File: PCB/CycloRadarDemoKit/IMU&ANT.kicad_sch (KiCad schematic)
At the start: 18 parts, among them J101 ANT_SWD, U302 D52MxxM8, U402 MPU-6050

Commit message: JLCPCB mistakes repaired, cosmetics on PCB
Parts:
- C103: LCSC C14663 -> (none)
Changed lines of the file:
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@@
-      (effects (font (size 1.27 1.27)) hide)
-    )
-    (property "LCSC" "C14663" (at 121.92 57.15 0)
       (effects (font (size 1.27 1.27)) hide)
     )

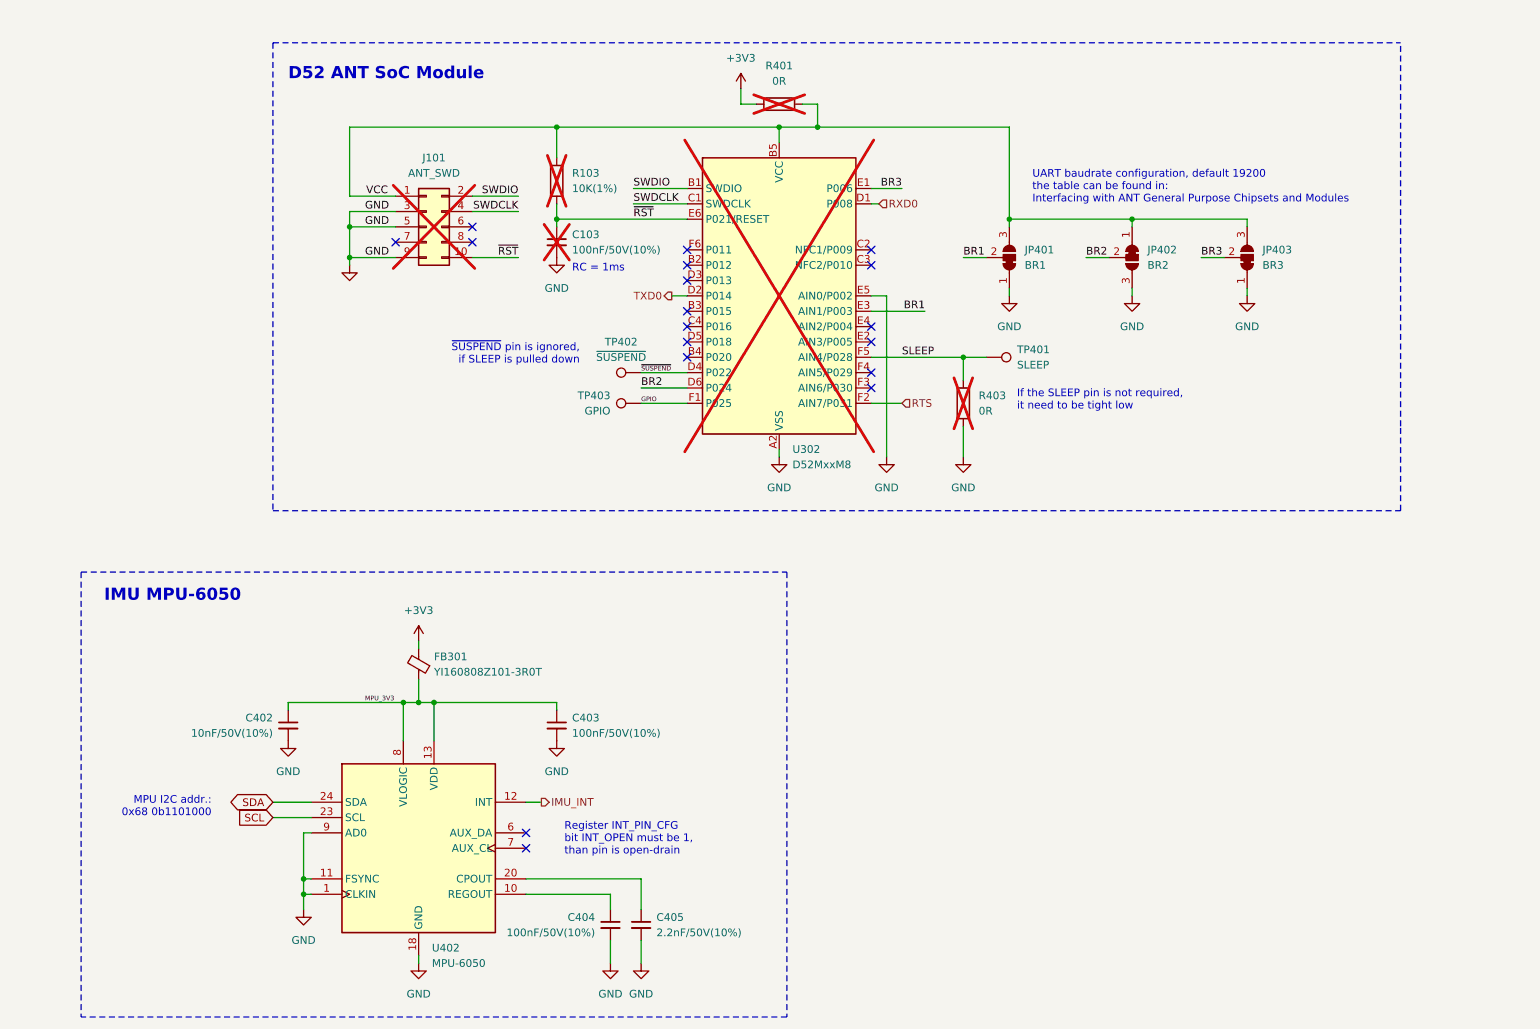
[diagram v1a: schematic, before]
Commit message: Sematic Versioning implemented, whish list added
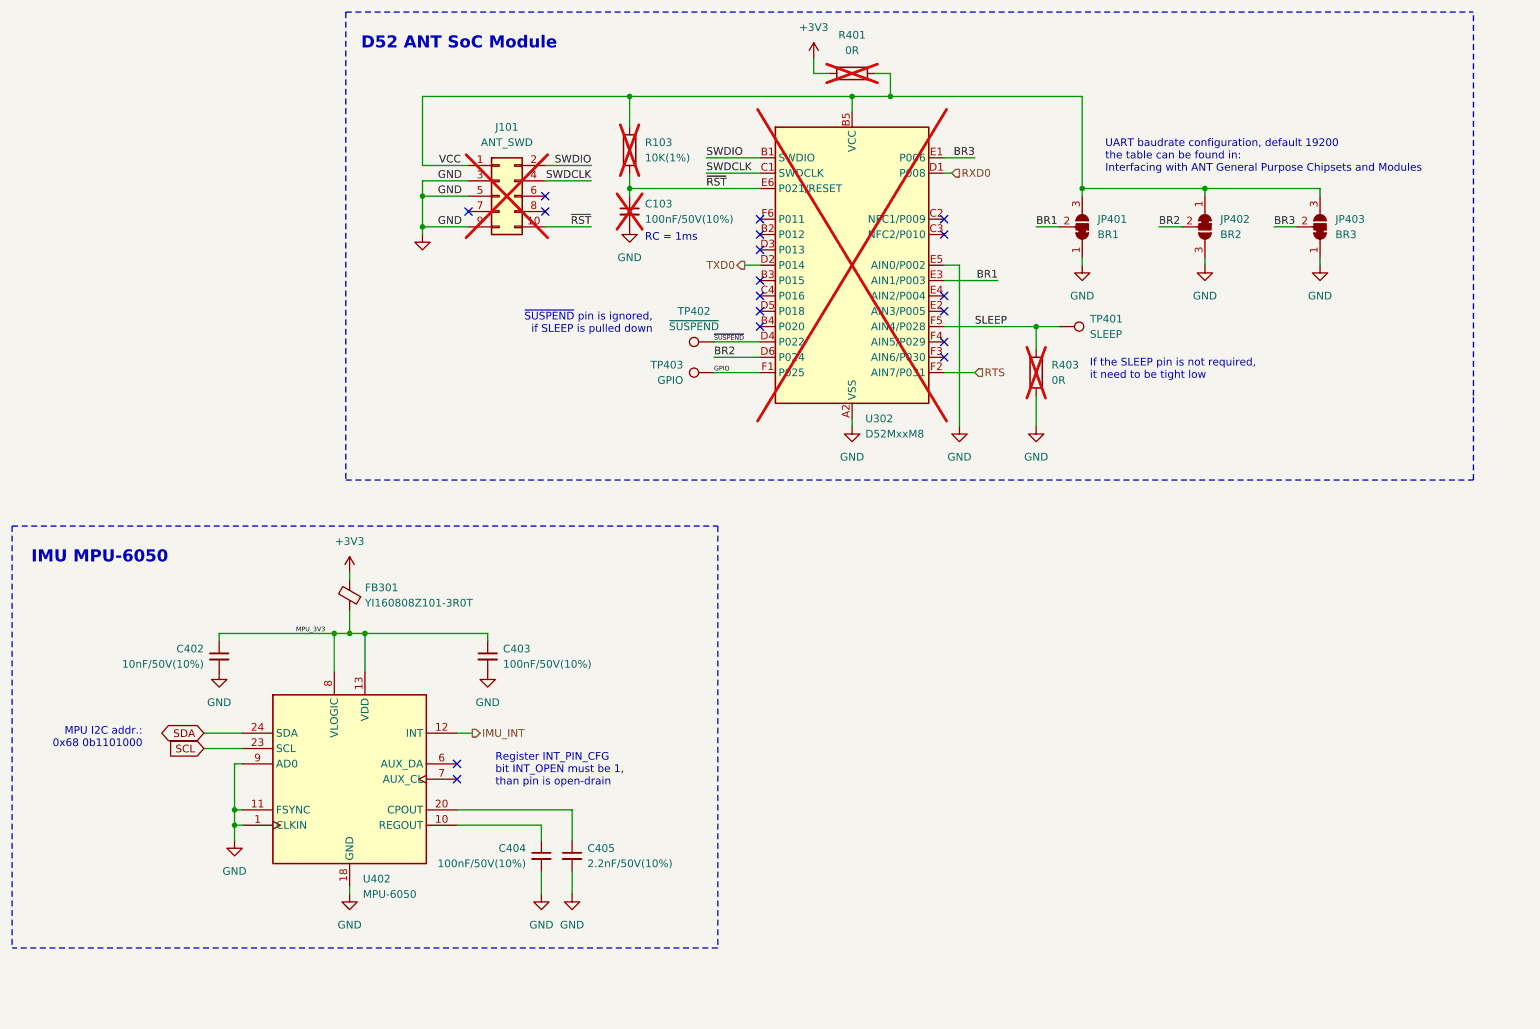
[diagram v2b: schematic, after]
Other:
- company: ALPS Electric Czech, s.r.o. -> ${COMPANY}
- title: Radar Safety Sensor -> ${TITLE}
- moved on the sheet: C103, C402, C403, C404, C405, FB301, J101, JP401, JP402, JP403, R103, R401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

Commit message: photos added, readme rewrited
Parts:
- renumbered C103 to C401, FB301 to FB401, J101 to J401, R103 to R402, U302 to U401
